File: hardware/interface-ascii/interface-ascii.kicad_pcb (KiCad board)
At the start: 2 copper layers, 88.9 x 132.1 mm, 48 parts, among them J1 Apple 2, J2 Apple 1, J3 UART, J4 Outputs, J5 ISP header, J6 Keyboard, J7 SOL-20, SW1 Options, U1 ATmega328P, U2 74LS166, U3 74LS138, U4 74LS138, U5 74LS04

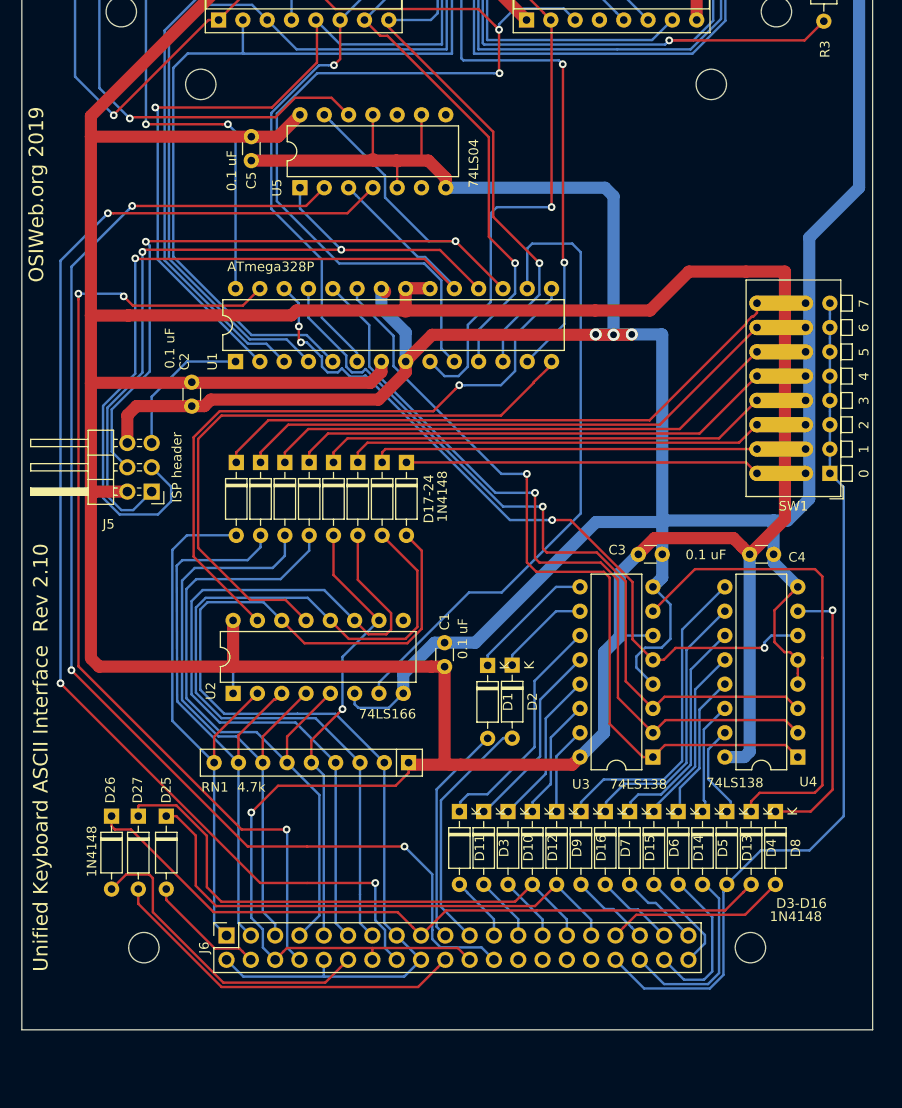
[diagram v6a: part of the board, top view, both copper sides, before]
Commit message: Fix shunted diode footprints on encoder boards
The encoder boards (ATmega328P, Atmega2560, Apple2(2560) can accomodate
keyboard matrices with no diodes, by adding per-row diodes on the
encoder board.  For keyboards with per-key diodes (the typical use
case), the per-row diodes are not needed, and therefore the footprints
should be shunted by default, using a special shunted diode footprint.
When diodes are installed, the shunt can be cut with an x-acto knife.
Previous board revs had the correct footprint, but somehow the regular
diode footprint was substituted on the last release of each of these
PCBS.  The correct footprint has been restored.
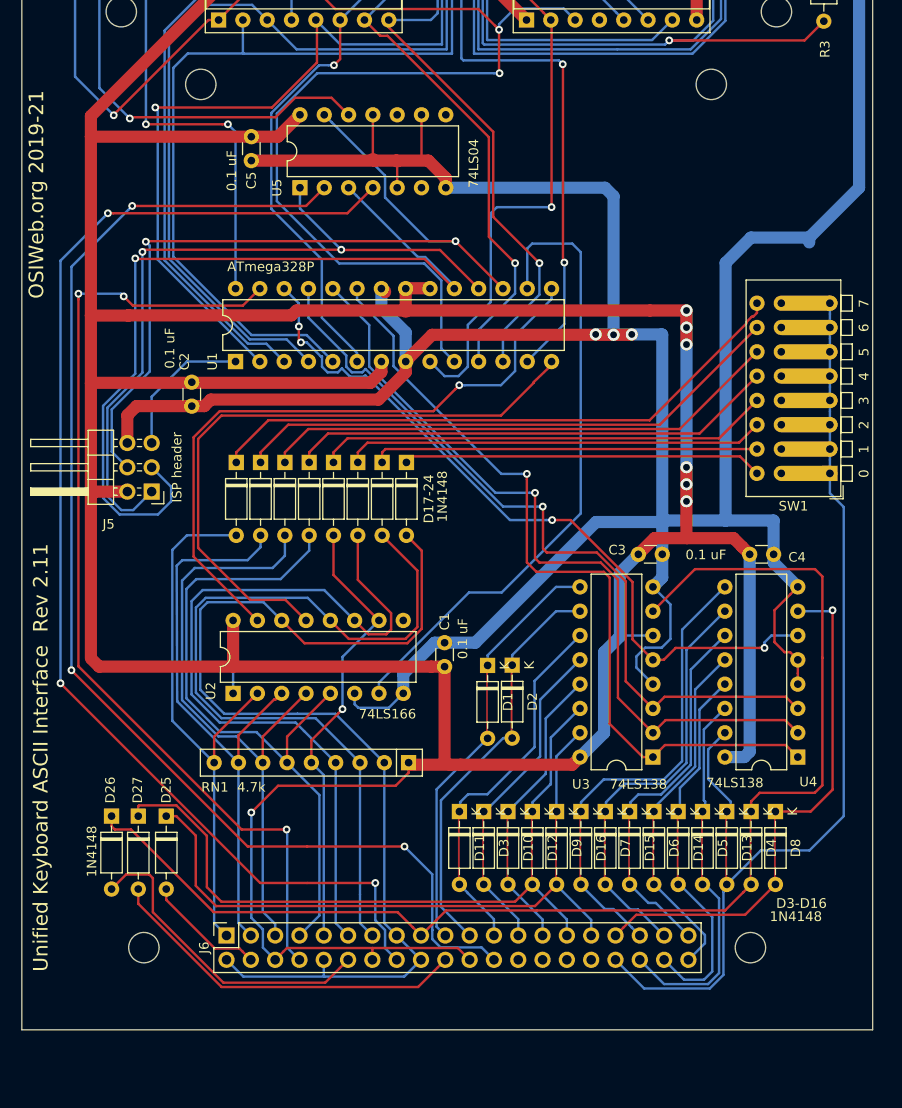
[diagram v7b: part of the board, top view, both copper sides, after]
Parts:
- D1, D10, D11, D12, D13, D14, D15, D16, D2, D3, D4, D5, D6, D7, D8, D9: footprint Diode_THT:D_DO-35_SOD27_P7.62mm_Horizontal -> unikbd:D_DO-35_SOD27_P7.62mm_Horizontal_bypassed
- SW1: footprint unikbd:SW_DIP_SPSTx08_Piano_CTS_Series194-8MSTN_W7.62mm_P2.54mm -> unikbd:SW_DIP_SPSTx08_oriented_backward
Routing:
- net +5V: track 569.1 -> 557.0 mm, vias 1 -> 7
- net GND: track 476.2 -> 481.5 mm
- net Net-(D17-Pad1): track 37.1 -> 37.6 mm
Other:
- board text added: "OSIWeb.org 2019-21"
- board text added: "Unified Keyboard ASCII Interface Rev 2.11"
- board text removed: "OSIWeb.org 2019"
- board text removed: "Unified Keyboard ASCII Interface Rev 2.10"
